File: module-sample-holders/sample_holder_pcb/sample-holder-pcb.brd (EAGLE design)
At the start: 35 x 35 mm, 12 parts, among them IC1 25AA040ST, IC2 DSPIC33CK256MP502-I_SS, Q1 PSMN013-30MLC, Q2 PSMN013-30MLC

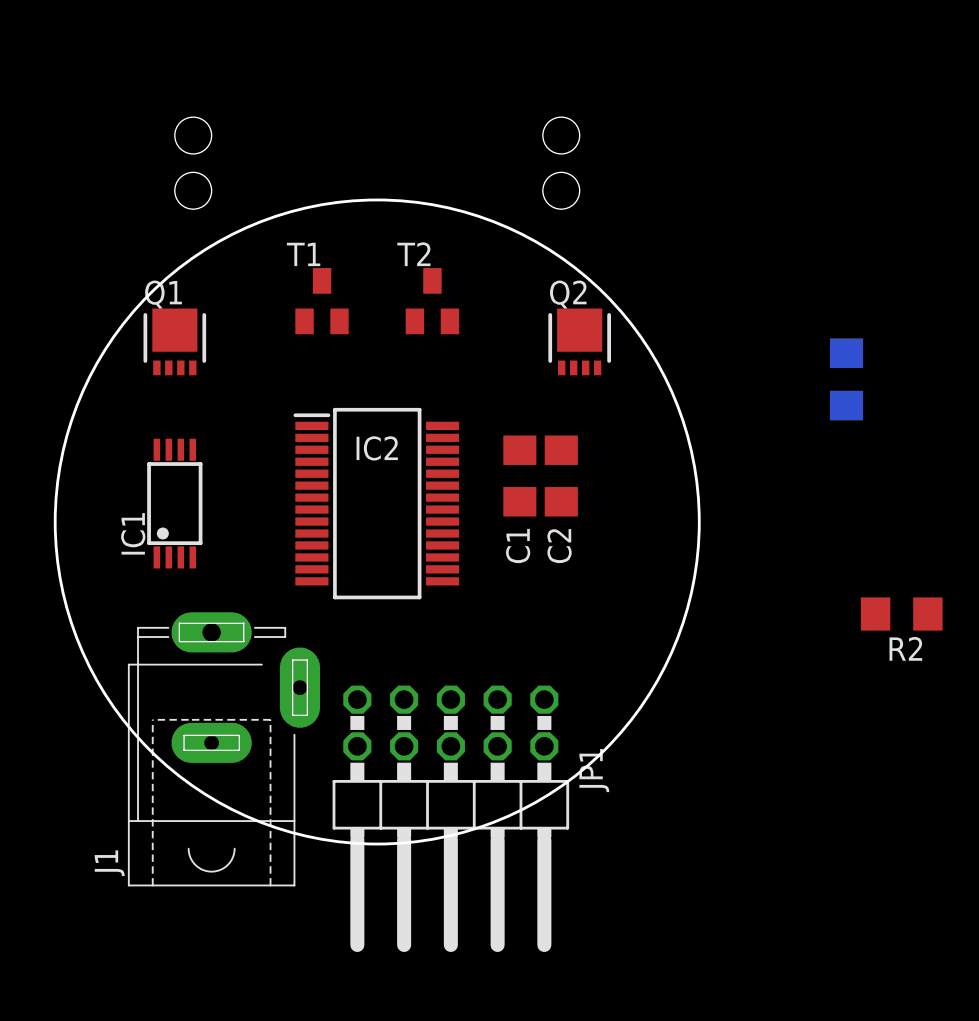
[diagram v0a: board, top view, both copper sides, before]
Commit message: Submitting old PCB design before replacing with new design.
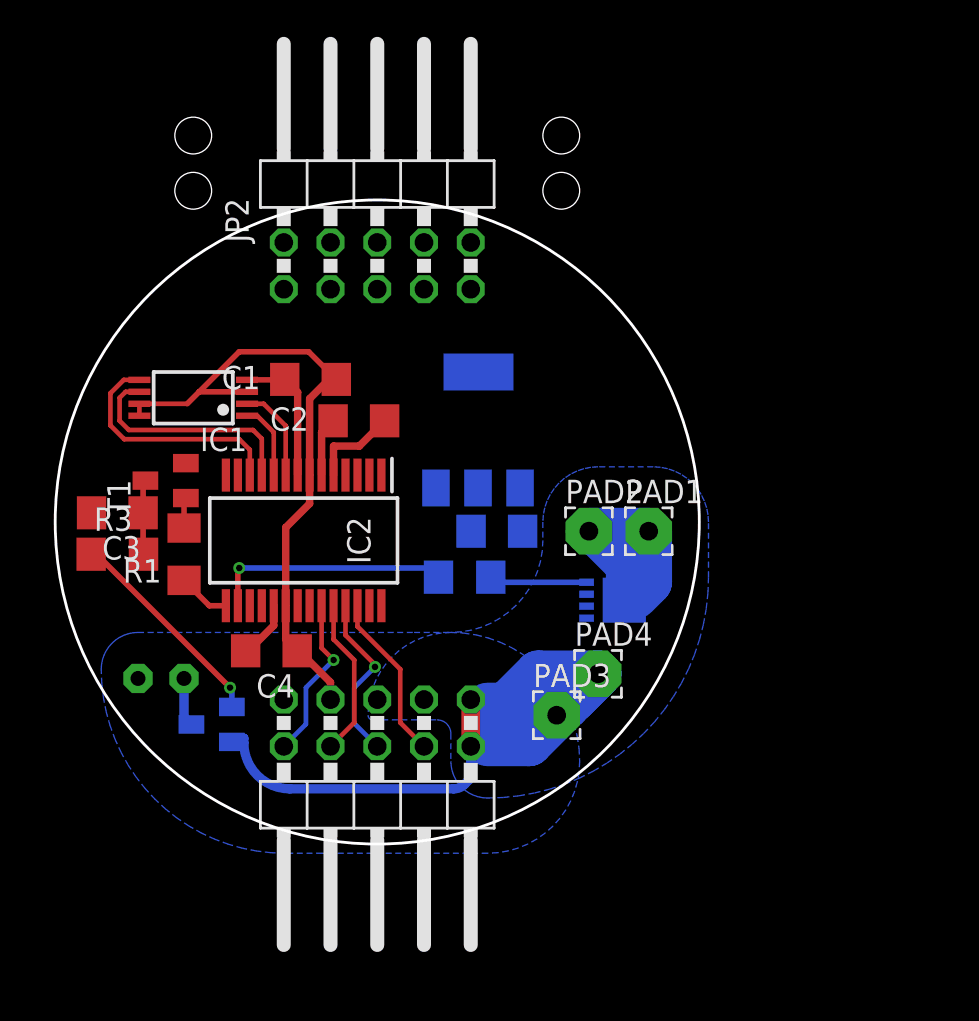
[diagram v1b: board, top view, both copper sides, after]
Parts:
- removed J1: (no value), con-jack:SPC4078
- removed Q2: PSMN013-30MLC, transistor-power:LFPAK33
- added C3, C4, C5: (no value), rcl:C1206
- added FAN_PWR_GND, FAN_PWR_OUT: (no value), wirepad:1,6/0,8
- added IC3: REG1117, burr-brown:SOT223
- added JP2: (no value), pinhead:2X05/90
- added PAD1, PAD2, PAD3, PAD4: (no value), wirepad:2,54/1,0
- added R3: (no value), rcl:R1206
- moved R1 37.2 mm to (23.5, 30.2), flipped to the top
- moved Q1 27.9 mm to (47.0, 27.8), flipped to the bottom, turned to 90 degrees
- moved T2 25.9 mm to (25.0, 21.0), flipped to the bottom, turned to 270 degrees
- moved R2 23.8 mm to (38.8, 29.0), flipped to the bottom, turned to 0 degrees
- moved T1 12.9 mm to (22.5, 34.2), turned to 90 degrees
- moved C1 12.5 mm to (30.4, 39.8), turned to 180 degrees
- moved C2 11.4 mm to (33.0, 37.5), turned to 180 degrees
- moved IC1 5.84 mm to (24.0, 38.8), turned to 90 degrees
- moved IC2 4.47 mm to (30.0, 31.0), turned to 270 degrees
- moved JP1 4.00 mm to (34.0, 16.0)
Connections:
- removed net VCC: IC1.8
- new net +12V: IC3.3, JP1.1, JP1.2, PAD3.1, PAD4.1, T2.E
- new net FAN_PWR_OUT: FAN_PWR_OUT.1, T2.C
- new net N$1: Q1.4, R2.1
- new net N$10: C3.1, R3.2, T1.C
- new net N$11: R3.1, T2.B
- new net N$12: IC2.23, JP1.10
- new net N$13: IC2.24, JP1.8
- new net N$14: IC2.25, JP1.6
- new net N$15: IC2.26, JP1.4
- new net N$16: IC2.15, R1.2
- new net N$17: IC2.16, R2.2
- new net N$2: IC1.6, IC2.11
- new net N$3: IC1.2, IC2.9
- new net N$4: IC1.1, IC2.10
- new net N$5: IC1.5, IC2.12
- new net N$8: PAD1.1, PAD2.1, Q1.MB
- new net N$9: R1.1, T1.B
- net GND: now also C3.2, C4.2, C5.2, FAN_PWR_GND.1, IC3.1, JP1.3, JP1.5, Q1.1, Q1.2, Q1.3, T1.E
- net V+: now also C4.1, C5.1, IC1.3, IC1.7, IC1.8, IC3.2, JP1.7
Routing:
- net +12V: track 0.00 -> 42.9 mm
- net V+: track 0.00 -> 40.5 mm
- net GND: track 0.00 -> 13.9 mm
- net N$5: track 0.00 -> 13.1 mm
- net N$17: track 0.00 -> 13.1 mm, vias 0 -> 1
- net N$2: track 0.00 -> 12.6 mm
- net N$11: track 0.00 -> 11.6 mm, vias 0 -> 1
- net N$8: track 0.00 -> 10.9 mm
- net N$14: track 0.00 -> 9.29 mm, vias 0 -> 1
- net N$15: track 0.00 -> 9.14 mm
- net N$12: track 0.00 -> 9.03 mm, vias 0 -> 1
- net N$13: track 0.00 -> 8.64 mm
- net N$1: track 0.00 -> 5.32 mm
- net N$3: track 0.00 -> 5.27 mm
- net N$4: track 0.00 -> 4.15 mm
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- added copper zone on layer 16, net GND

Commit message: Sample Holder new design, first PCB submitted for manufacture.
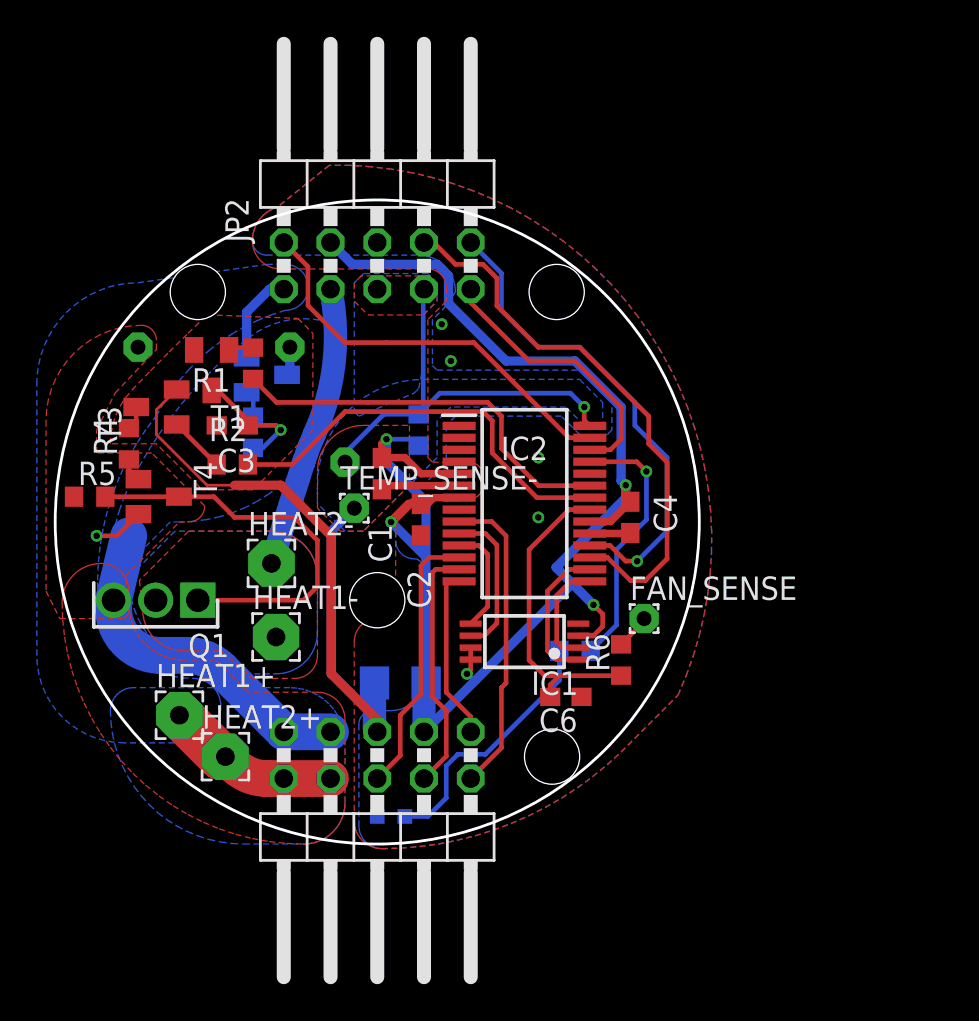
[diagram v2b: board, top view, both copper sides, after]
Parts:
- removed FAN_PWR_GND, FAN_PWR_OUT: (no value), wirepad:1,6/0,8
- removed IC3: REG1117, burr-brown:SOT223
- removed PAD1, PAD2, PAD3, PAD4: (no value), wirepad:2,54/1,0
- added C6: (no value), rcl:C0603
- added FAN+, FAN-, FAN_SENSE, TEMP_SENSE+, TEMP_SENSE-: (no value), wirepad:1,6/0,8
- added HEAT1+, HEAT1-, HEAT2+, HEAT2-: (no value), wirepad:2,54/1,0
- added LED1: (no value), led:SML0603
- added R4, R5, R6, R7, R8: (no value), rcl:R0603
- added T3, T4: (no value), transistor:SOT23-BEC
- C1, C2, C3, C4: device rcl:C1206 -> rcl:C0603
- Q1: value PSMN013-30MLC -> AUIRFU8403; device transistor-power:LFPAK33 -> AUIRFU8403:TO229P239X654X978-3P
- R1, R2, R3: device rcl:R1206 -> rcl:R0603
- moved Q1 22.8 mm to (24.2, 27.8), flipped to the top, turned to 180 degrees
- moved IC1 22.4 mm to (42.0, 25.5)
- moved C4 20.8 mm to (47.8, 32.2), turned to 270 degrees
- moved T2 19.2 mm to (28.0, 40.0), turned to 90 degrees
- moved R2 14.0 mm to (26.1, 35.1), flipped to the top
- moved IC2 12.2 mm to (42.0, 33.0), turned to 0 degrees
- moved R1 11.0 mm to (27.2, 40.6)
- moved R3 9.91 mm to (27.2, 36.9), flipped to the bottom, turned to 270 degrees
- moved C5 9.78 mm to (35.2, 23.2), turned to 0 degrees
- moved C3 7.85 mm to (26.1, 37.2)
- moved T1 6.50 mm to (25.0, 40.2), turned to 180 degrees
- moved C1 6.43 mm to (34.2, 34.6), turned to 270 degrees
- moved C2 6.35 mm to (36.4, 32.1), turned to 270 degrees
- moved JP1 1.75 mm to (34.0, 14.2)
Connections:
- removed net FAN_PWR_OUT: FAN_PWR_OUT.1, T2.C
- removed net N$8: PAD1.1, PAD2.1, Q1.MB
- removed net V+: C1.1, C2.1, C4.1, C5.1, IC1.3, IC1.7, IC1.8, IC2.20, IC2.5, IC2.7, IC3.2, JP1.7
- new net +3V3: C1.1, C2.1, C4.1, C5.1, IC1.3, IC1.7, IC1.8, IC2.20, IC2.5, IC2.7, JP1.3, JP2.4, R7.1
- new net 0V: FAN-.1, JP1.7, JP1.9, Q1.3, R5.1
- new net FAN+: FAN+.1, T2.C
- new net FAN_SENSE: C6.2, IC2.21, R6.1
- new net HEAT-: HEAT1-.1, HEAT2-.1, JP2.3, Q1.2
- new net MCLR: IC2.27, JP2.2
- new net N$6: LED1.A, R8.2
- new net N$7: IC2.25, R8.1
- new net PGC: IC2.18, JP2.10
- new net PGD: IC2.17, JP2.8
- new net SPI1: IC2.9, JP1.2
- new net SPI2: IC2.12, JP1.6
- new net SPI3: IC2.13, JP1.4
- new net SPI4: IC2.14, JP1.1
- new net TEMP_SENSE: IC2.28, JP2.7, R7.2, TEMP_SENSE+.1
- new net TX: IC2.26, JP2.9
- net +12V: now also HEAT1+.1, HEAT2+.1, JP1.10, JP1.8, JP2.1, T4.E; no longer IC3.3, JP1.1, JP1.2, PAD3.1, PAD4.1
- net GND: now also C6.1, JP2.5, JP2.6, LED1.C, T3.E, TEMP_SENSE-.1; no longer FAN_PWR_GND.1, IC3.1, JP1.3, Q1.1, Q1.2, Q1.3
- net N$1: now also T3.B; no longer Q1.4
- net N$12: now also IC2.22, R2.2; no longer IC2.23, JP1.10
- net N$13: now also IC1.5, IC2.11; no longer IC2.24, JP1.8
- net N$14: now also IC1.6, IC2.10; no longer IC2.25, JP1.6
- net N$15: now also IC1.2, IC2.15; no longer IC2.26, JP1.4
- net N$16: now also IC1.1, IC2.16; no longer IC2.15, R1.2
- net N$17: now also IC2.23, R1.2; no longer IC2.16, R2.2
- net N$2: now also R4.2, T3.C; no longer IC1.6, IC2.11
- net N$3: now also R4.1, T4.B; no longer IC1.2, IC2.9
- net N$4: now also Q1.1, R5.2, T4.C; no longer IC1.1, IC2.10
- net N$5: now also FAN_SENSE.1, R6.2; no longer IC1.5, IC2.12
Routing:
- net +3V3: track 0.00 -> 85.1 mm, vias 0 -> 5
- net V+: track 40.5 -> 0.00 mm
- net GND: track 13.9 -> 49.3 mm, vias 0 -> 4
- net PGD: track 0.00 -> 30.4 mm
- net PGC: track 0.00 -> 26.7 mm, vias 0 -> 1
- net +12V: track 42.9 -> 17.2 mm, vias 0 -> 1
- net TEMP_SENSE: track 0.00 -> 23.2 mm, vias 0 -> 1
- net MCLR: track 0.00 -> 22.3 mm
- net 0V: track 0.00 -> 18.5 mm
- net N$4: track 4.15 -> 21.8 mm
- net FAN_SENSE: track 0.00 -> 16.9 mm
- net SPI1: track 0.00 -> 16.9 mm
- net HEAT-: track 0.00 -> 15.4 mm
- net TX: track 0.00 -> 14.9 mm
- net SPI2: track 0.00 -> 14.8 mm
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- added copper zone on layer 16, net +12V
- added copper zone on layer 1, net 0V
- added copper zone on layer 16, net 0V
- added copper zone on layer 1, net GND
- added copper zone on layer 1, net HEAT-
- added copper zone on layer 16, net HEAT-

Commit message: Minor changes to PCB: 1mm larger, MCLR resistor + cap added, thicker trace to external heater.  Second manufacturing, not express.
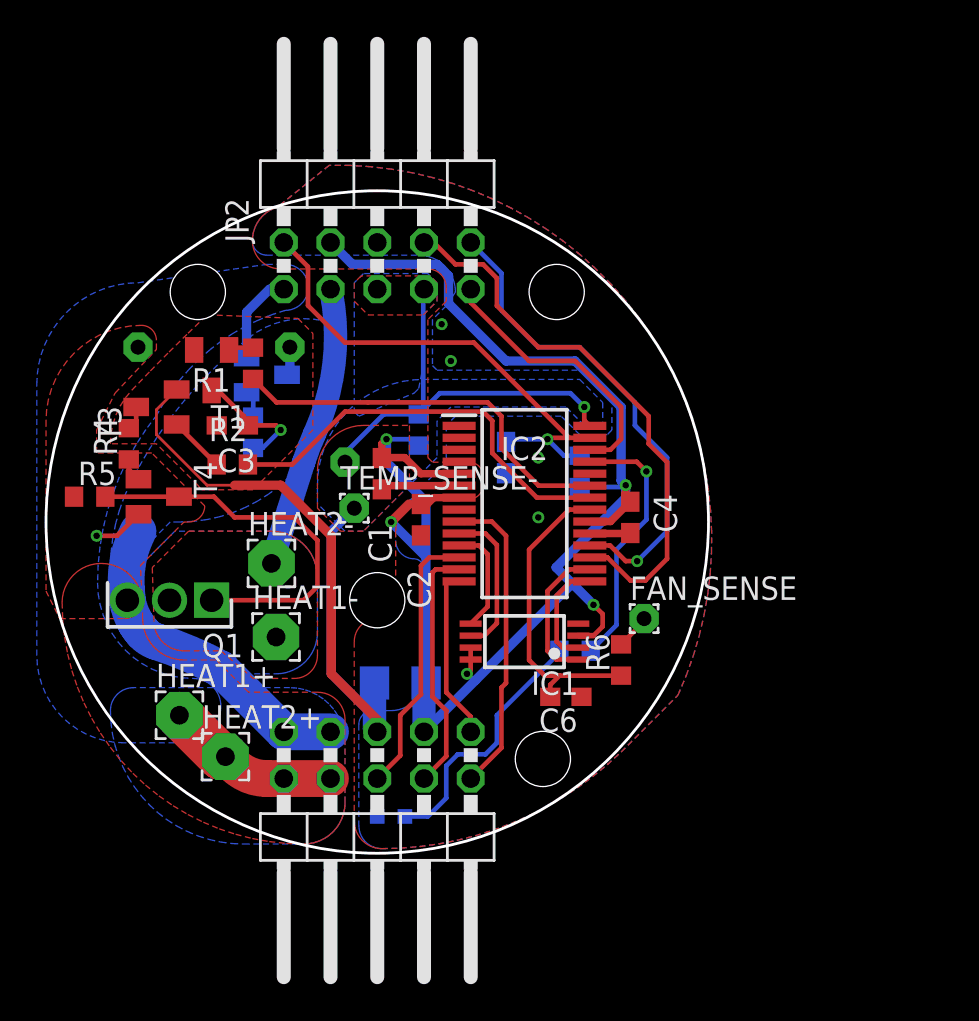
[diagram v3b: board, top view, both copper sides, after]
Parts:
- added C7: (no value), rcl:C0603
- added R9: 10k, rcl:R0603
- C1, C2, C4, C6: value (none) -> 100nf
- C3: value (none) -> 1nf
- C5: value (none) -> 10uf
- R1, R2, R3, R4, R5, R6: value (none) -> 1k
- R7: value (none) -> 3.3k
- R8: value (none) -> 120
- moved Q1 0.75 mm to (25.0, 27.8)
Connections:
- net +3V3: now also R9.1
- net GND: now also C7.1
- net MCLR: now also C7.2, R9.2
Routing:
- net MCLR: track 22.3 -> 27.9 mm, vias 0 -> 1
- net +3V3: track 85.1 -> 87.6 mm
- net N$4: track 21.8 -> 21.1 mm
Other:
- board size 35 x 35 mm -> 36 x 36 mm

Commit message: Changed fan sense resistor from 1k to 510, because at low speed the fan feedback would not pull low enough.
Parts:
- R6: value 1k -> 510R
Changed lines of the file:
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@@
 <?xml version="1.0" encoding="utf-8"?>
 <!DOCTYPE eagle SYSTEM "eagle.dtd">
-<eagle version="9.5.2">
+<eagle version="9.5.1">
 <drawing>
 <settings>
@@
 <attribute name="VALUE" x="48.5" y="27.35" size="0.0254" layer="27"/>
 </element>
-<element name="R6" library="rcl" library_urn="urn:adsk.eagle:library:334" package="R0603" package3d_urn="urn:adsk.eagle:package:23555/3" value="1k" x="47.25" y="24.5" smashed="yes" rot="R90">
+<element name="R6" library="rcl" library_urn="urn:adsk.eagle:library:334" package="R0603" package3d_urn="urn:adsk.eagle:package:23555/3" value="510R" x="47.25" y="24.5" smashed="yes" rot="R90">
 <attribute name="NAME" x="46.615" y="23.865" size="1.27" layer="25" rot="R90"/>
 <attribute name="SPICEPREFIX" value="R" x="47.25" y="24.5" size="1.778" layer="27" rot="R90" display="off"/>

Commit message: Added SPI names.
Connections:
- net SPI1 renamed SPI_SS
- net SPI2 renamed SPI_MISO
- net SPI3 renamed SPI_MOSI
- net SPI4 renamed SPI_CLK
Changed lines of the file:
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@@
 <wire x1="47.25" y1="38.25" x2="47.25" y2="36.50486875" width="0.254" layer="1"/>
 </signal>
-<signal name="SPI1">
+<signal name="SPI_SS">
 <contactref element="IC2" pad="9"/>
 <contactref element="JP1" pad="2"/>
@@
 <wire x1="40.75" y1="19.73" x2="40.75" y2="23" width="0.254" layer="1"/>
 </signal>
-<signal name="SPI2">
+<signal name="SPI_MISO">
 <contactref element="IC2" pad="12"/>
 <contactref element="JP1" pad="6"/>
@@
 <wire x1="35.25" y1="21.5" x2="36.375" y2="22.625" width="0.254" layer="1"/>
 </signal>
-<signal name="SPI3">
+<signal name="SPI_MOSI">
 <contactref element="IC2" pad="13"/>
 <contactref element="JP1" pad="4"/>
@@
 <wire x1="37" y1="29.25" x2="37.175" y2="29.425" width="0.254" layer="1"/>
 </signal>
-<signal name="SPI4">
+<signal name="SPI_CLK">
 <contactref element="IC2" pad="14"/>
 <contactref element="JP1" pad="1"/>
